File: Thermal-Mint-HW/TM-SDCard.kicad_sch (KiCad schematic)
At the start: 1 part, among them J1 Molex_5031821852

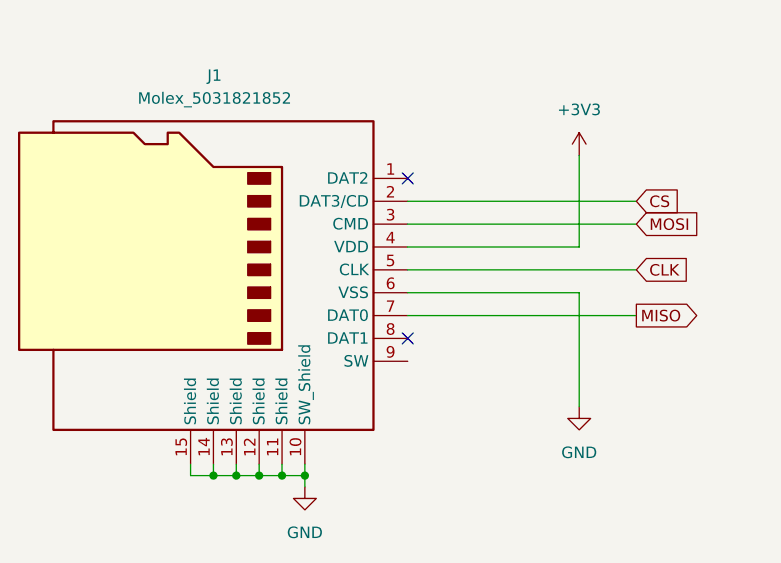
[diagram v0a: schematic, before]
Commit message: WIP commit, Adding connectors and memory
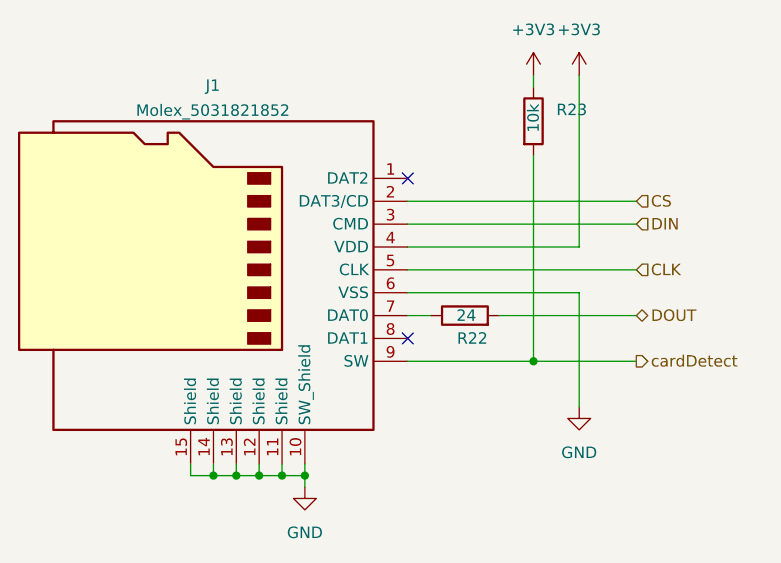
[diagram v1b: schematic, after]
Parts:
- added R22: 24, Resistor_SMD:R_0603_1608Metric_Pad0.98x0.95mm_HandSolder, symbol Device:R
- added R23: 10k, Resistor_SMD:R_0603_1608Metric_Pad0.98x0.95mm_HandSolder, symbol Device:R
- J1: footprint CH:Molex_SDCard_5031821852 -> ThermalMint:Molex_SDCard_5031821852
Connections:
- net +3V3: now also R23.1
- net cardDetect: now reaches J1.9 (SW)
- net cardDetect: now also R23.2
- net MISO: no longer names the net of J1.7 (DAT0)
- net MISO: now also R22.1
- net MOSI renamed DIN
- new net DOUT: R22.2

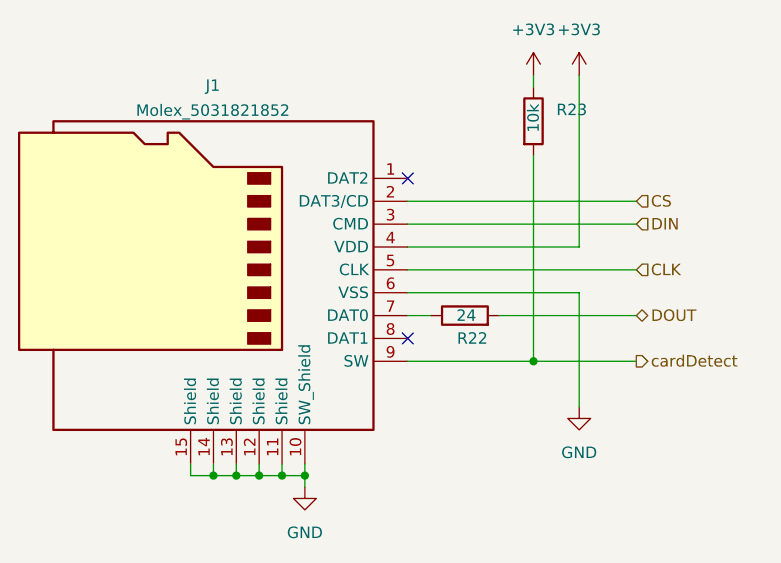
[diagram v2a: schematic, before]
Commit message: Cleanup of Rev1 schematics for review
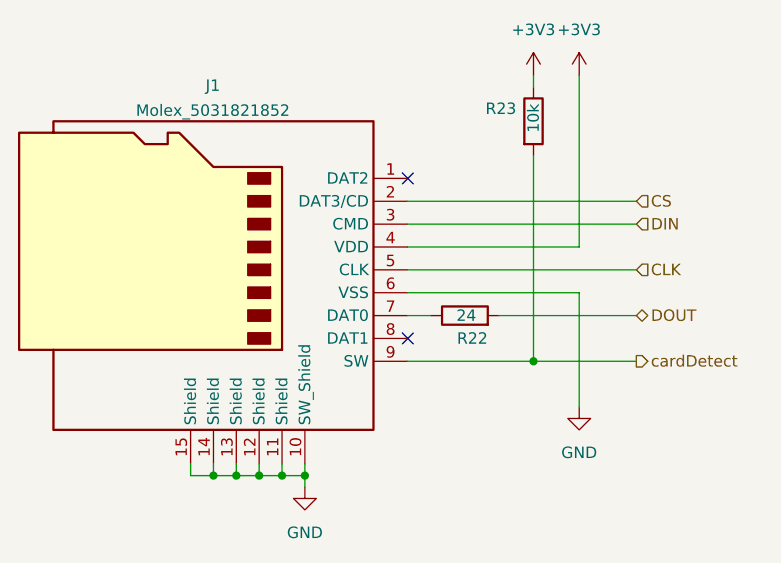
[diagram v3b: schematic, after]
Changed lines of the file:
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@@
   (symbol (lib_id "Device:R") (at 176.53 88.9 0) (unit 1)
     (in_bom yes) (on_board yes)
-    (property "Reference" "R23" (id 0) (at 179.07 87.6299 0)
+    (property "Reference" "R23" (id 0) (at 171.196 87.503 0)
       (effects (font (size 1.27 1.27)) (justify left))
     )
